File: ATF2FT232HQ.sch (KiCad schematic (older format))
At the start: 15 parts, among them J1 FT232HQ-Shield, J2 JTAG, SW1 SW_SPST, U1 ATF1504AS-10JU44, U2 MAX662A

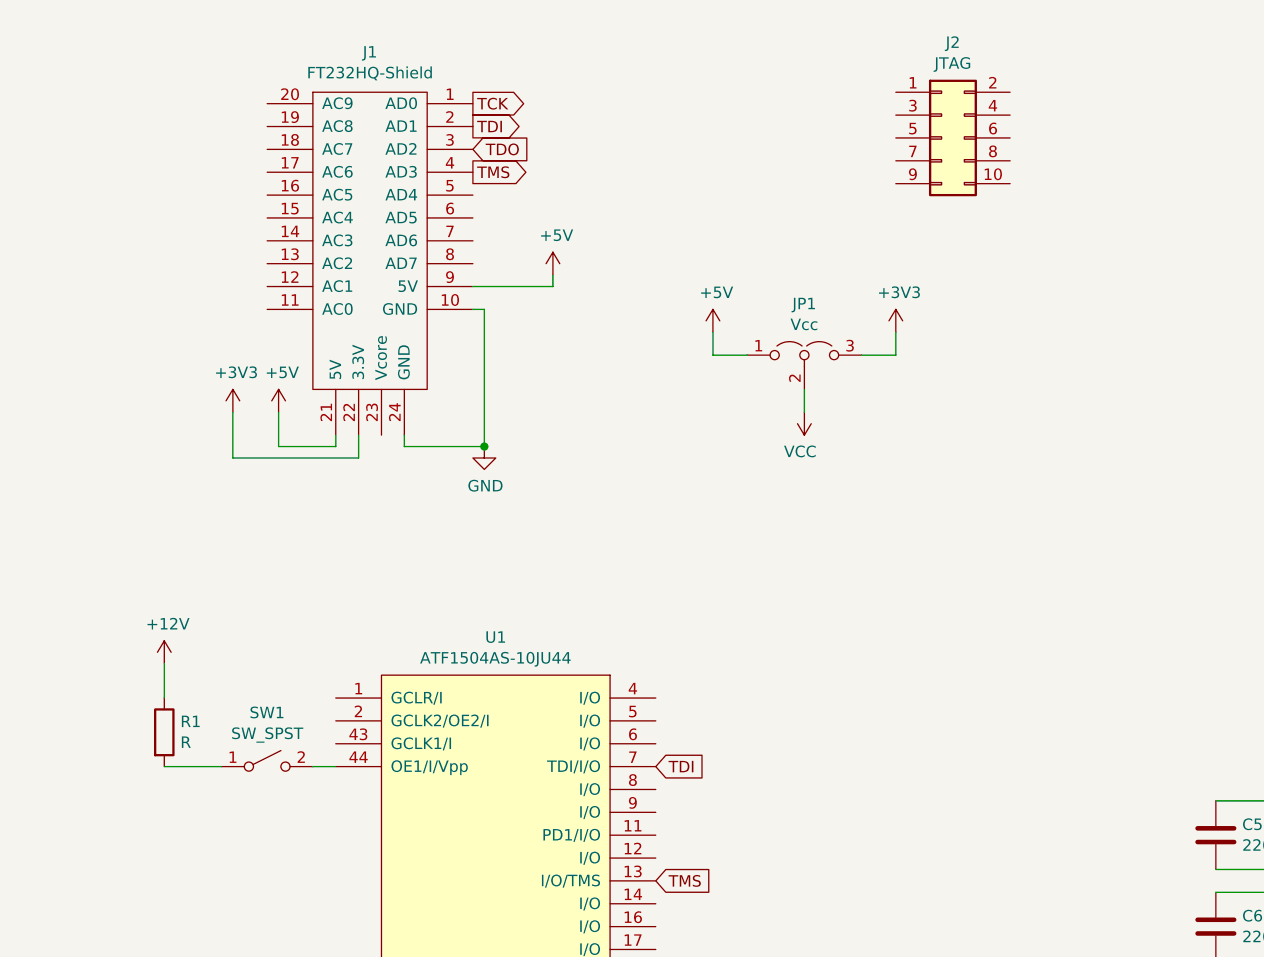
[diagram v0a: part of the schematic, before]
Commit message: First routing completed.
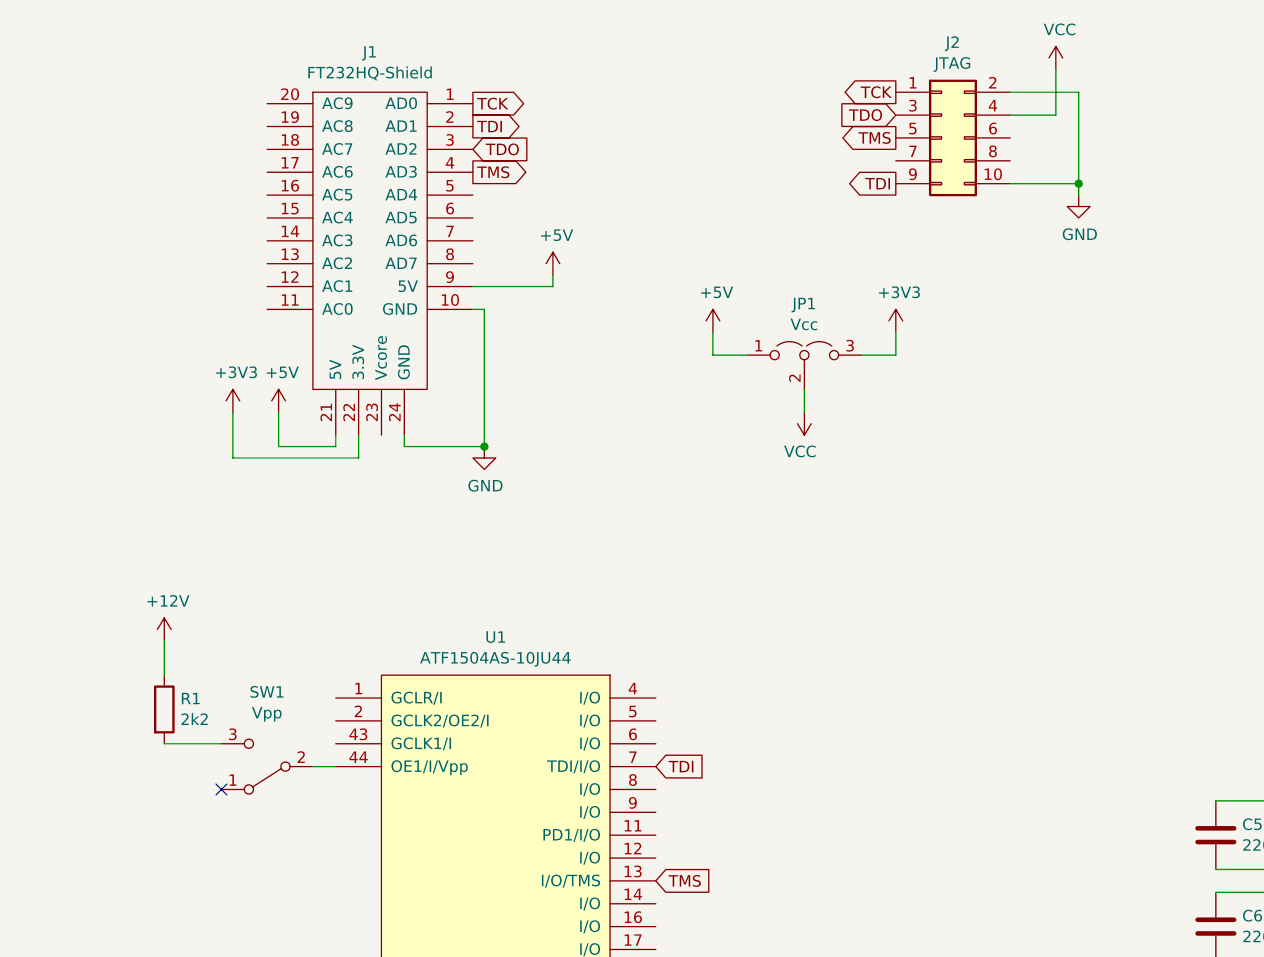
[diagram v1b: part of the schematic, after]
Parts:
- removed SW1: SW_SPST, Connector_PinHeader_2.54mm:PinHeader_1x02_P2.54mm_Vertical, symbol Switch:SW_SPST
- added SW1: Vpp, Button_Switch_THT:SW_Slide_1P2T_CK_OS102011MS2Q, symbol Switch:SW_SPDT
- R1: value R -> 2k2
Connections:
- net GND: now also J2.10 (Pin_10), J2.2 (Pin_2)
- net TCK: now also J2.1 (Pin_1)
- net TDI: now also J2.9 (Pin_9)
- net TDO: now also J2.3 (Pin_3)
- net TMS: now also J2.5 (Pin_5)
- net VCC: now also J2.4 (Pin_4)
- net at U1.44 (OE1/I/Vpp): now also SW1.2 (B)
- net at R1.2: now also SW1.3 (C)
- no-connect marks 0 -> 1
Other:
- moved on the sheet: R1
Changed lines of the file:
@@
 Text GLabel 3550 4100 2    50   Input ~ 0
 TDI
-$Comp
-L Switch:SW_SPST SW1
-U 1 1 5DD24D2E
-P 1850 4100
-F 0 "SW1" H 1850 4335 50  0000 C CNN
-F 1 "SW_SPST" H 1850 4244 50  0000 C CNN
-F 2 "Connector_PinHeader_2.54mm:PinHeader_1x02_P2.54mm_Vertical" H 1850 4100 50  0001 C CNN
-F 3 "~" H 1850 4100 50  0001 C CNN
-	1    1850 4100
-	1    0    0    -1
-$EndComp
 Wire Wire Line
 	2050 4100 2150 4100
@@
 L Device:R R1
 U 1 1 5DD25F42
-P 1400 3950
-F 0 "R1" H 1470 3996 50  0000 L CNN
-F 1 "R" H 1470 3905 50  0000 L CNN
-F 2 "Resistor_SMD:R_0805_2012Metric_Pad1.15x1.40mm_HandSolder" V 1330 3950 50  0001 C CNN
-F 3 "~" H 1400 3950 50  0001 C CNN
-	1    1400 3950
+P 1400 3850
+F 0 "R1" H 1470 3896 50  0000 L CNN
+F 1 "2k2" H 1470 3805 50  0000 L CNN
+F 2 "Resistor_SMD:R_0805_2012Metric_Pad1.15x1.40mm_HandSolder" V 1330 3850 50  0001 C CNN
+F 3 "~" H 1400 3850 50  0001 C CNN
+	1    1400 3850
 	1    0    0    -1
 $EndComp
@@
 L power:+12V #PWR0107
 U 1 1 5DD26EB6
-P 1400 3650
-F 0 "#PWR0107" H 1400 3500 50  0001 C CNN
-F 1 "+12V" H 1415 3823 50  0000 C CNN
-F 2 "" H 1400 3650 50  0001 C CNN
-F 3 "" H 1400 3650 50  0001 C CNN
-	1    1400 3650
-	1    0    0    -1
-$EndComp
-Wire Wire Line
-	1400 3650 1400 3800
-Wire Wire Line
-	1400 4100 1650 4100
+P 1400 3550
+F 0 "#PWR0107" H 1400 3400 50  0001 C CNN
+F 1 "+12V" H 1415 3723 50  0000 C CNN
+F 2 "" H 1400 3550 50  0001 C CNN
+F 3 "" H 1400 3550 50  0001 C CNN
+	1    1400 3550
+	1    0    0    -1
+$EndComp
+Wire Wire Line
+	1400 3550 1400 3700
+Wire Wire Line
+	1400 4000 1650 4000
 $Comp
 L Device:C C1
@@
 Wire Wire Line
 	4200 2450 4200 2550
+$Comp
+L Switch:SW_SPDT SW1
+U 1 1 5DD534AC
+P 1850 4100
+F 0 "SW1" H 1850 3775 50  0000 C CNN
+F 1 "Vpp" H 1850 3866 50  0000 C CNN
+F 2 "Button_Switch_THT:SW_Slide_1P2T_CK_OS102011MS2Q" H 1850 4100 50  0001 C CNN
+F 3 "~" H 1850 4100 50  0001 C CNN
+	1    1850 4100
+	-1   0    0    1
+$EndComp
+NoConn ~ 1650 4200
+Text GLabel 4600 1150 0    50   Output ~ 0
+TCK
+Text GLabel 4600 1550 0    50   Output ~ 0
+TDI
+Text GLabel 4600 1250 0    50   Input ~ 0
+TDO
+Text GLabel 4600 1350 0    50   Output ~ 0
+TMS
+$Comp
+L power:GND #PWR?
+U 1 1 5DD5F3CC
+P 5400 1600
+F 0 "#PWR?" H 5400 1350 50  0001 C CNN
+F 1 "GND" H 5405 1427 50  0000 C CNN
+F 2 "" H 5400 1600 50  0001 C CNN
+F 3 "" H 5400 1600 50  0001 C CNN
+	1    5400 1600
+	1    0    0    -1
+$EndComp
+$Comp
+L power:VCC #PWR?
+U 1 1 5DD5FAAA
+P 5300 1050
+F 0 "#PWR?" H 5300 900 50  0001 C CNN
+F 1 "VCC" H 5318 1223 50  0000 C CNN
+F 2 "" H 5300 1050 50  0001 C CNN
+F 3 "" H 5300 1050 50  0001 C CNN
+	1    5300 1050
+	1    0    0    -1
+$EndComp
+Wire Wire Line
+	5100 1250 5300 1250
+Wire Wire Line
+	5300 1250 5300 1050
+Wire Wire Line
+	5100 1150 5400 1150
+Wire Wire Line
+	5400 1150 5400 1550
+Wire Wire Line
+	5100 1550 5400 1550
+Connection ~ 5400 1550
+Wire Wire Line
+	5400 1550 5400 1600
 $EndSCHEMATC

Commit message: Moved components to the top.
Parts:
- SW1: footprint Button_Switch_THT:SW_Slide_1P2T_CK_OS102011MS2Q -> Connector_PinHeader_2.54mm:PinHeader_1x03_P2.54mm_Vertical
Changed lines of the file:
@@
 F 0 "SW1" H 1850 3775 50  0000 C CNN
 F 1 "Vpp" H 1850 3866 50  0000 C CNN
-F 2 "Button_Switch_THT:SW_Slide_1P2T_CK_OS102011MS2Q" H 1850 4100 50  0001 C CNN
+F 2 "Connector_PinHeader_2.54mm:PinHeader_1x03_P2.54mm_Vertical" H 1850 4100 50  0001 C CNN
 F 3 "~" H 1850 4100 50  0001 C CNN
 	1    1850 4100
@@
 TMS
 $Comp
-L power:GND #PWR?
+L power:GND #PWR0115
 U 1 1 5DD5F3CC
 P 5400 1600
-F 0 "#PWR?" H 5400 1350 50  0001 C CNN
+F 0 "#PWR0115" H 5400 1350 50  0001 C CNN
 F 1 "GND" H 5405 1427 50  0000 C CNN
 F 2 "" H 5400 1600 50  0001 C CNN
@@
 $EndComp
 $Comp
-L power:VCC #PWR?
+L power:VCC #PWR0116
 U 1 1 5DD5FAAA
 P 5300 1050
-F 0 "#PWR?" H 5300 900 50  0001 C CNN
+F 0 "#PWR0116" H 5300 900 50  0001 C CNN
 F 1 "VCC" H 5318 1223 50  0000 C CNN
 F 2 "" H 5300 1050 50  0001 C CNN

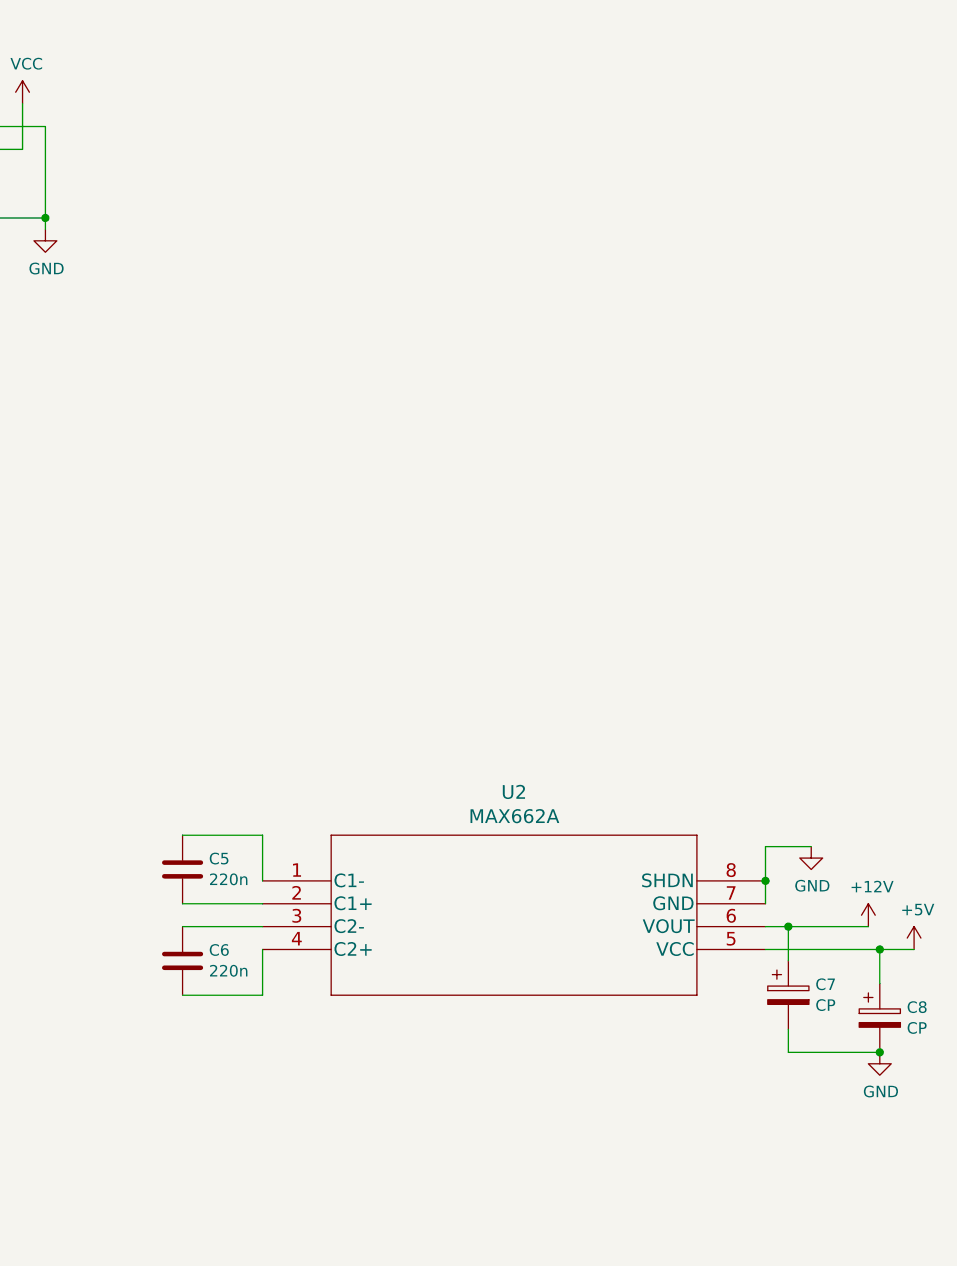
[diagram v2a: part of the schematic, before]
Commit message: Updated MAX662 footprint.
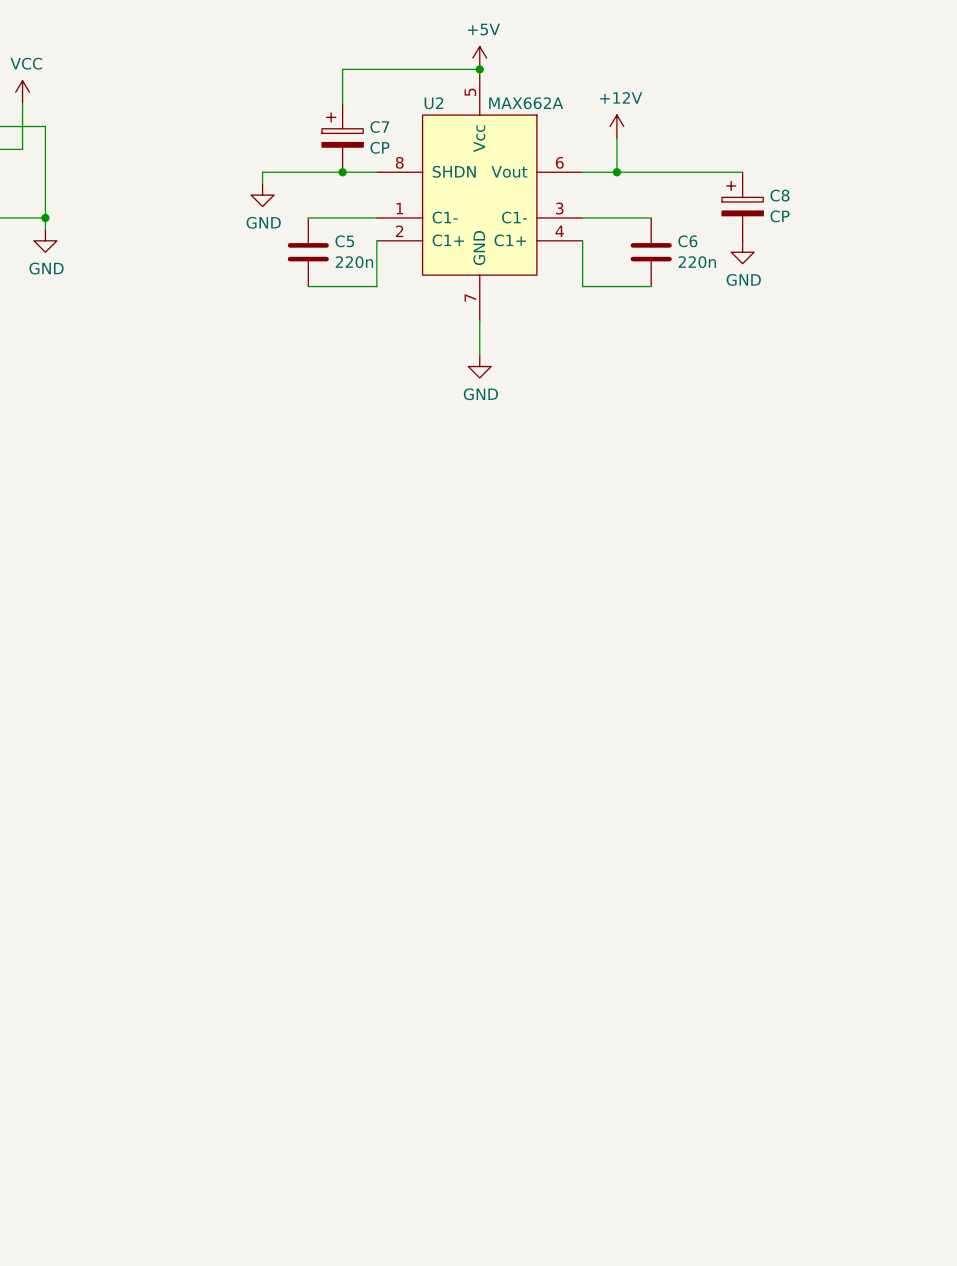
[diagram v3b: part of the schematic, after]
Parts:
- removed U2: MAX662A, max662:MAX662ACSA&plus_, symbol max662:MAX662ACSA+
- added U2: MAX662A, Package_SO:SOIC-8_3.9x4.9mm_P1.27mm, symbol max662:MAX662A
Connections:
- net +12V: now also C8.1, U2.6 (Vout); no longer C7.1
- net +5V: now also C7.1, U2.5 (Vcc); no longer C8.1
- net GND: now also U2.7 (GND), U2.8 (SHDN)
- net at C5.1: now also U2.1 (C1-)
- net at C5.2: now also U2.2 (C1+)
- net at C6.1: now also U2.3 (C1-)
- net at C6.2: now also U2.4 (C1+)
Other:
- moved on the sheet: C5, C6, C7, C8
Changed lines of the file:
@@
 encoding utf-8
 Sheet 1 1
-Title ""
-Date ""
-Rev ""
-Comp ""
+Title "ATF1504 - FT232HQ Adapter Shield"
+Date "2019-11-20"
+Rev "1"
+Comp "hackup.net"
 Comment1 ""
 Comment2 ""
@@
 $EndComp
 $Comp
-L max662:MAX662ACSA+ U2
-U 1 1 5DD4354C
-P 6350 4450
-F 0 "U2" H 7450 4837 60  0000 C CNN
-F 1 "MAX662A" H 7450 4731 60  0000 C CNN
-F 2 "max662:MAX662ACSA&plus_" H 7450 4690 60  0001 C CNN
-F 3 "" H 6350 4450 60  0000 C CNN
-	1    6350 4450
-	1    0    0    -1
-$EndComp
-$Comp
 L Device:C C3
 U 1 1 5DD48530
@@
 L Device:C C5
 U 1 1 5DD5AA55
-P 6000 4400
-F 0 "C5" H 6115 4446 50  0000 L CNN
-F 1 "220n" H 6115 4355 50  0000 L CNN
-F 2 "Capacitor_SMD:C_0805_2012Metric_Pad1.15x1.40mm_HandSolder" H 6038 4250 50  0001 C CNN
-F 3 "~" H 6000 4400 50  0001 C CNN
-	1    6000 4400
+P 6550 1700
+F 0 "C5" H 6665 1746 50  0000 L CNN
+F 1 "220n" H 6665 1655 50  0000 L CNN
+F 2 "Capacitor_SMD:C_0805_2012Metric_Pad1.15x1.40mm_HandSolder" H 6588 1550 50  0001 C CNN
+F 3 "~" H 6550 1700 50  0001 C CNN
+	1    6550 1700
 	1    0    0    -1
 $EndComp
@@
 L Device:C C6
 U 1 1 5DD5B407
-P 6000 4800
-F 0 "C6" H 6115 4846 50  0000 L CNN
-F 1 "220n" H 6115 4755 50  0000 L CNN
-F 2 "Capacitor_SMD:C_0805_2012Metric_Pad1.15x1.40mm_HandSolder" H 6038 4650 50  0001 C CNN
-F 3 "~" H 6000 4800 50  0001 C CNN
-	1    6000 4800
-	1    0    0    -1
-$EndComp
-Wire Wire Line
-	6350 4650 6000 4650
-Wire Wire Line
-	6000 4550 6350 4550
-Wire Wire Line
-	6350 4450 6350 4250
-Wire Wire Line
-	6350 4250 6000 4250
-Wire Wire Line
-	6000 4950 6350 4950
-Wire Wire Line
-	6350 4950 6350 4750
-$Comp
-L power:GND #PWR0108
-U 1 1 5DD603BC
-P 8750 4300
-F 0 "#PWR0108" H 8750 4050 50  0001 C CNN
-F 1 "GND" H 8755 4127 50  0000 C CNN
-F 2 "" H 8750 4300 50  0001 C CNN
-F 3 "" H 8750 4300 50  0001 C CNN
-	1    8750 4300
-	1    0    0    -1
-$EndComp
-Wire Wire Line
-	8550 4550 8550 4450
-Wire Wire Line
-	8550 4300 8750 4300
-Connection ~ 8550 4450
-Wire Wire Line
-	8550 4450 8550 4300
+P 8050 1700
+F 0 "C6" H 8165 1746 50  0000 L CNN
+F 1 "220n" H 8165 1655 50  0000 L CNN
+F 2 "Capacitor_SMD:C_0805_2012Metric_Pad1.15x1.40mm_HandSolder" H 8088 1550 50  0001 C CNN
+F 3 "~" H 8050 1700 50  0001 C CNN
+	1    8050 1700
+	1    0    0    -1
+$EndComp
 $Comp
 L power:+12V #PWR0109
 U 1 1 5DD61929
-P 9000 4650
-F 0 "#PWR0109" H 9000 4500 50  0001 C CNN
-F 1 "+12V" H 9015 4823 50  0000 C CNN
-F 2 "" H 9000 4650 50  0001 C CNN
-F 3 "" H 9000 4650 50  0001 C CNN
-	1    9000 4650
+P 7900 1200
+F 0 "#PWR0109" H 7900 1050 50  0001 C CNN
+F 1 "+12V" H 7915 1373 50  0000 C CNN
+F 2 "" H 7900 1200 50  0001 C CNN
+F 3 "" H 7900 1200 50  0001 C CNN
+	1    7900 1200
 	1    0    0    -1
 $EndComp
@@
 L power:+5V #PWR0110
 U 1 1 5DD61F2E
-P 9200 4750
-F 0 "#PWR0110" H 9200 4600 50  0001 C CNN
-F 1 "+5V" H 9215 4923 50  0000 C CNN
-F 2 "" H 9200 4750 50  0001 C CNN
-F 3 "" H 9200 4750 50  0001 C CNN
-	1    9200 4750
-	1    0    0    -1
-$EndComp
-Wire Wire Line
-	8550 4650 8650 4650
-Wire Wire Line
-	8550 4750 9050 4750
+P 7300 900
+F 0 "#PWR0110" H 7300 750 50  0001 C CNN
+F 1 "+5V" H 7315 1073 50  0000 C CNN
+F 2 "" H 7300 900 50  0001 C CNN
+F 3 "" H 7300 900 50  0001 C CNN
+	1    7300 900
+	1    0    0    -1
+$EndComp
 $Comp
 L Device:CP C7
 U 1 1 5DD649DB
-P 8650 4950
-F 0 "C7" H 8768 4996 50  0000 L CNN
-F 1 "CP" H 8768 4905 50  0000 L CNN
-F 2 "Capacitor_Tantalum_SMD:CP_EIA-3216-18_Kemet-A_Pad1.58x1.35mm_HandSolder" H 8688 4800 50  0001 C CNN
-F 3 "~" H 8650 4950 50  0001 C CNN
-	1    8650 4950
+P 6700 1200
+F 0 "C7" H 6818 1246 50  0000 L CNN
+F 1 "CP" H 6818 1155 50  0000 L CNN
+F 2 "Capacitor_Tantalum_SMD:CP_EIA-3216-18_Kemet-A_Pad1.58x1.35mm_HandSolder" H 6738 1050 50  0001 C CNN
+F 3 "~" H 6700 1200 50  0001 C CNN
+	1    6700 1200
 	1    0    0    -1
 $EndComp
@@
 L Device:CP C8
 U 1 1 5DD65E61
-P 9050 5050
-F 0 "C8" H 9168 5096 50  0000 L CNN
-F 1 "CP" H 9168 5005 50  0000 L CNN
-F 2 "Capacitor_Tantalum_SMD:CP_EIA-3216-18_Kemet-A_Pad1.58x1.35mm_HandSolder" H 9088 4900 50  0001 C CNN
-F 3 "~" H 9050 5050 50  0001 C CNN
-	1    9050 5050
-	1    0    0    -1
-$EndComp
-Wire Wire Line
-	8650 4800 8650 4650
-Connection ~ 8650 4650
-Wire Wire Line
-	8650 4650 9000 4650
-Wire Wire Line
-	9050 4900 9050 4750
-Connection ~ 9050 4750
-Wire Wire Line
-	9050 4750 9200 4750
+P 8450 1500
+F 0 "C8" H 8568 1546 50  0000 L CNN
+F 1 "CP" H 8568 1455 50  0000 L CNN
+F 2 "Capacitor_Tantalum_SMD:CP_EIA-3216-18_Kemet-A_Pad1.58x1.35mm_HandSolder" H 8488 1350 50  0001 C CNN
+F 3 "~" H 8450 1500 50  0001 C CNN
+	1    8450 1500
+	1    0    0    -1
+$EndComp
 $Comp
 L power:GND #PWR0111
 U 1 1 5DD68572
-P 9050 5200
-F 0 "#PWR0111" H 9050 4950 50  0001 C CNN
-F 1 "GND" H 9055 5027 50  0000 C CNN
-F 2 "" H 9050 5200 50  0001 C CNN
-F 3 "" H 9050 5200 50  0001 C CNN
-	1    9050 5200
-	1    0    0    -1
-$EndComp
-Wire Wire Line
-	8650 5100 8650 5200
-Wire Wire Line
-	8650 5200 9050 5200
-Connection ~ 9050 5200
+P 8450 1650
+F 0 "#PWR0111" H 8450 1400 50  0001 C CNN
+F 1 "GND" H 8455 1477 50  0000 C CNN
+F 2 "" H 8450 1650 50  0001 C CNN
+F 3 "" H 8450 1650 50  0001 C CNN
+	1    8450 1650
+	1    0    0    -1
+$EndComp
 $Comp
 L power:VCC #PWR0112
@@
 Wire Wire Line
 	5400 1550 5400 1600
+$Comp
+L max662:MAX662A U2
+U 1 1 5DD59DFC
+P 7300 1600
+F 0 "U2" H 7100 2150 50  0000 C CNN
+F 1 "MAX662A" H 7500 2150 50  0000 C CNN
+F 2 "Package_SO:SOIC-8_3.9x4.9mm_P1.27mm" H 7300 1350 50  0001 C CNN
+F 3 "" H 7300 1350 50  0001 C CNN
+	1    7300 1600
+	1    0    0    -1
+$EndComp
+Wire Wire Line
+	6550 1550 6850 1550
+Wire Wire Line
+	6550 1850 6850 1850
+Wire Wire Line
+	6850 1850 6850 1650
+Wire Wire Line
+	7750 1550 8050 1550
+Wire Wire Line
+	7750 1650 7750 1850
+Wire Wire Line
+	7750 1850 8050 1850
+$Comp
+L power:GND #PWR0108
+U 1 1 5DD631B4
+P 7300 2150
+F 0 "#PWR0108" H 7300 1900 50  0001 C CNN
+F 1 "GND" H 7305 1977 50  0000 C CNN
+F 2 "" H 7300 2150 50  0001 C CNN
+F 3 "" H 7300 2150 50  0001 C CNN
+	1    7300 2150
+	1    0    0    -1
+$EndComp
+$Comp
+L power:GND #PWR0117
+U 1 1 5DD636B0
+P 6350 1400
+F 0 "#PWR0117" H 6350 1150 50  0001 C CNN
+F 1 "GND" H 6355 1227 50  0000 C CNN
+F 2 "" H 6350 1400 50  0001 C CNN
+F 3 "" H 6350 1400 50  0001 C CNN
+	1    6350 1400
+	1    0    0    -1
+$EndComp
+Wire Wire Line
+	6350 1400 6350 1350
+Wire Wire Line
+	7300 2000 7300 2150
+Wire Wire Line
+	6350 1350 6700 1350
+Connection ~ 6700 1350
+Wire Wire Line
+	6700 1350 6850 1350
+Wire Wire Line
+	7750 1350 7900 1350
+Wire Wire Line
+	7900 1200 7900 1350
+Connection ~ 7900 1350
+Wire Wire Line
+	7900 1350 8450 1350
+Wire Wire Line
+	6700 1050 6700 900
+Wire Wire Line
+	6700 900  7300 900
+Connection ~ 7300 900
 $EndSCHEMATC

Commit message: Fix.
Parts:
- C7: value CP -> 3.7u
- C8: value CP -> 4.7u
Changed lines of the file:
@@
 P 6700 1200
 F 0 "C7" H 6818 1246 50  0000 L CNN
-F 1 "CP" H 6818 1155 50  0000 L CNN
+F 1 "3.7u" H 6818 1155 50  0000 L CNN
 F 2 "Capacitor_Tantalum_SMD:CP_EIA-3216-18_Kemet-A_Pad1.58x1.35mm_HandSolder" H 6738 1050 50  0001 C CNN
 F 3 "~" H 6700 1200 50  0001 C CNN
@@
 P 8450 1500
 F 0 "C8" H 8568 1546 50  0000 L CNN
-F 1 "CP" H 8568 1455 50  0000 L CNN
+F 1 "4.7u" H 8568 1455 50  0000 L CNN
 F 2 "Capacitor_Tantalum_SMD:CP_EIA-3216-18_Kemet-A_Pad1.58x1.35mm_HandSolder" H 8488 1350 50  0001 C CNN
 F 3 "~" H 8450 1500 50  0001 C CNN

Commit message: Fixed typo.
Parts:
- C7: value 3.7u -> 4.7u
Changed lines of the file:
@@
 EESchema Schematic File Version 4
-LIBS:ATF2FT232HQ-cache
 EELAYER 30 0
 EELAYER END
@@
 P 6700 1200
 F 0 "C7" H 6818 1246 50  0000 L CNN
-F 1 "3.7u" H 6818 1155 50  0000 L CNN
+F 1 "4.7u" H 6818 1155 50  0000 L CNN
 F 2 "Capacitor_Tantalum_SMD:CP_EIA-3216-18_Kemet-A_Pad1.58x1.35mm_HandSolder" H 6738 1050 50  0001 C CNN
 F 3 "~" H 6700 1200 50  0001 C CNN
